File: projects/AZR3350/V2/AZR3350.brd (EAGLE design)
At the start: 128 x 80.5 mm, 168 parts, among them IC1 LM2734Y, IC11 74HC125, IC2 LDO-TS1117CW-3V3, IC3 74S08D, IC5 A4988, IC6 A4988, IC7 A4988, IC8 A4988, IC9 SI87XXIS, J107 ZX62-AB-5PA, Q1 FDS6890A, Q2 IRF520, Q3 IRF520, X3 MSTBV4

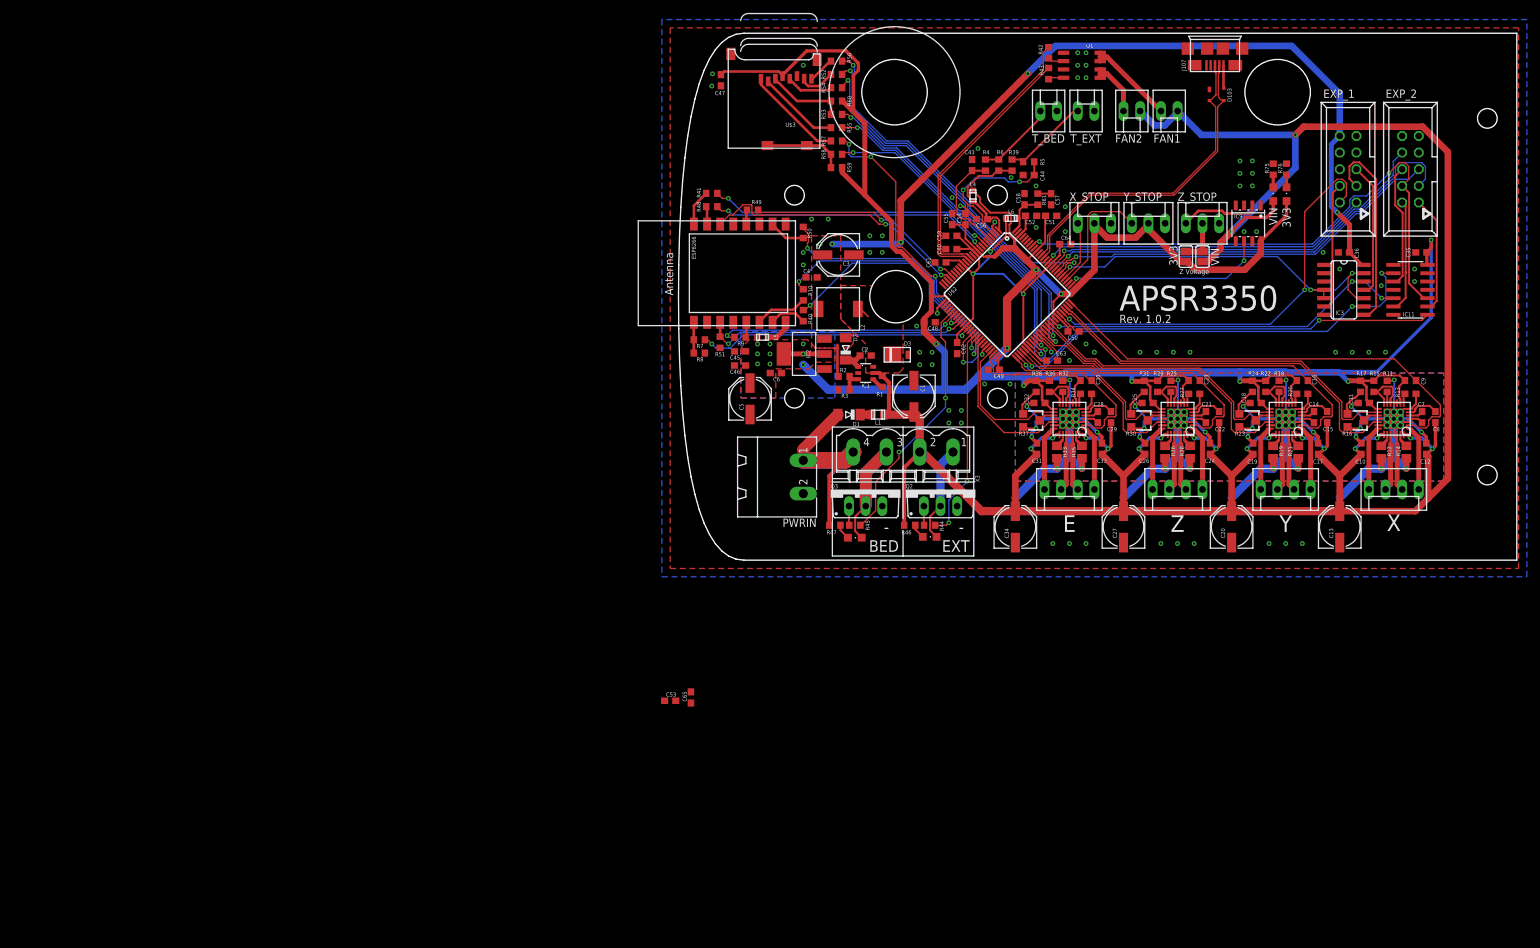
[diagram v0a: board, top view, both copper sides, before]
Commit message: Found all of the parts on DigiKey
(and replaced most that didn't work, for various reasons)
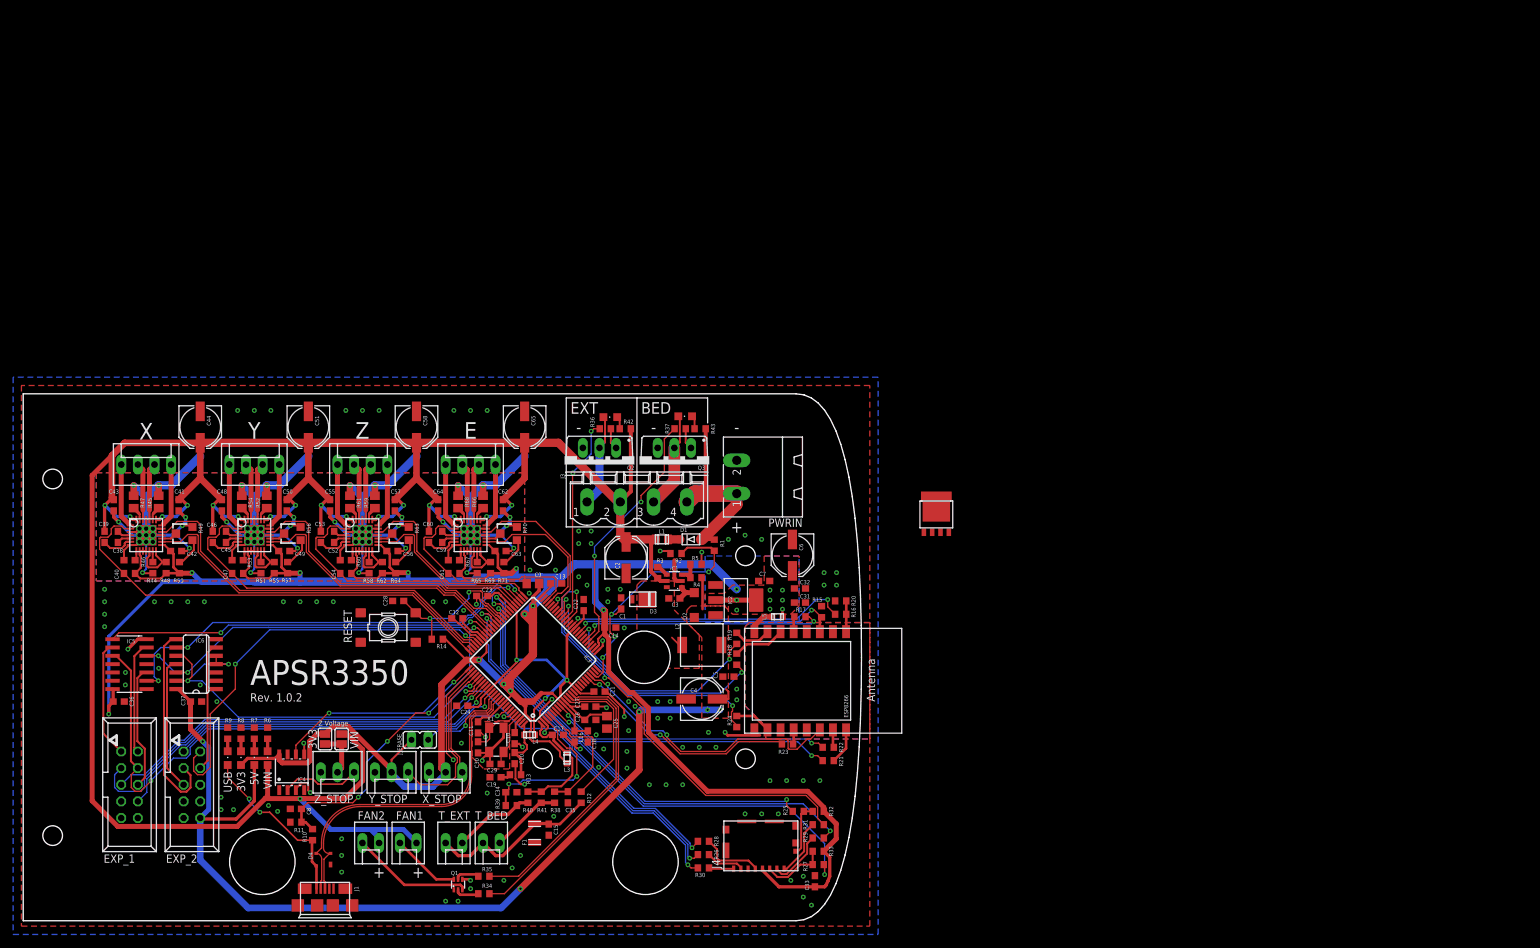
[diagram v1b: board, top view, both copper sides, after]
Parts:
- removed D103: PRTR5V0U2XB, Arduino:SOT143B
- removed IC11: 74HC125, misc:SO14
- removed J107: ZX62-AB-5PA, Arduino:USB-MICRO-10103594
- removed L6: 10uH 100MHz, Zero_V1.0:C0603
- removed R75: 4K7, resistor:R0603
- removed R76: 180R, resistor:R0603
- removed U$2: ATSAM4S8C, misc:LQFP100
- removed U$3: MICROSD, adafruit:MICROSD
- removed X3: MSTBV4, con-phoenix-508:MSTBV4
- added 5V, USB: (no value), led:CHIPLED_0805
- added C37, C38, C39, C41: 100n, resistor:C0603
- added C40, C42: 220n, resistor:C0603
- added D4: PRTR5V0U2XB, Arduino:SOT143B
- added F1: MC36207, misc:MC36207
- added IC10: A4988, RepRapjr:QFN28-TP
- added IC4: SI87XXIS, misc:SOIC08-FAIRCHILD
- added J1: ZX62-AB-5PA, Arduino:USB-MICRO-10103594
- added J3: MSTBV4, con-phoenix-508:MSTBV4
- added J4: MOLEX-105162-001, misc:MOLEX-105162
- added J_ERASE: (no value), jumper:JP1
- added L3: 10uH 100MHz, Zero_V1.0:C0603
- added Q4: BUK9Y53-100B, misc:SOT-669
- added R62, R69: 100K, resistor:R0603
- added R63, R70: 10K, resistor:RTRIM3103
- added R64, R71: 20K, resistor:R0603
- added R65, R67: 10K, resistor:R0603
- added R66, R68: 0R2, resistor:R0805
- added RESET: (no value), Zero_V1.0:TS42_4PINS
- added X1: 12MHz, misc:5.0X3.2_KX-9A
- C1: value 10uF -> 10n; device resistor:PANASONIC_D -> resistor:C0603
- C11, C16, C23: value 220n -> 100n
- C13, C20: value 100u -> 100n; device resistor:PANASONIC_D -> resistor:C0603
- C15, C36: value 100n -> 2.2u
- C18, C32: value 220n -> 10u
- C19: value 100n -> 4u7
- C2: value 10n -> 10uF; device resistor:C0603 -> resistor:PANASONIC_D
- C25, C9: value 220n -> 10u; device resistor:C0603 -> resistor:C0805
- C27: value 100u -> 2.2u 0.1-10ohm ESR; device resistor:PANASONIC_D -> resistor:C0603
- C28: value 100n -> 10n
- C29: value 100n -> 10p
- C3: value 47u -> 100n; device resistor:PANASONIC_D -> resistor:C0603
- C30: value 220n -> 10p
- C31: value 100n -> 10u
- C33: value 100n -> 2K2
- C34: value 100u -> 2.2u; device resistor:PANASONIC_D -> resistor:C0603
- C4: value 4.7uF -> 47u; device resistor:C0603 -> resistor:PANASONIC_D
- C43: value 2.2u -> 100n
- C44: value 2.2u -> 100u; device resistor:C0603 -> resistor:PANASONIC_D
- C45, C46, C53, C55: value 10u -> 100n
- C47: value 2K2 -> 220n
- C49, C54, C56, C61, C63: value 100n -> 220n
- C5: value 10uF -> 4.7uF; device resistor:PANASONIC_D -> resistor:C0603
- C51, C58: value 100n -> 100u; device resistor:C0603 -> resistor:PANASONIC_D
- C57: value 4u7 -> 100n
- C6: value 4.7uF -> 10uF; device resistor:C0603 -> resistor:PANASONIC_D
- C60: value 2.2u 0.1-10ohm ESR -> 100n
- C65: value 10u -> 100u; device resistor:C0603 -> resistor:PANASONIC_D
- C7: value 100n -> 4.7uF
- D1: device Diodi:MINIMELF -> adafruit:SOD-123FL
- D2: device Diodi:MINIMELF -> diode:SOD123
- IC3: value 74S08D -> ATSAM4S8C; device 74xx-us:SO14 -> misc:LQFP100
- IC5: value A4988 -> 74HC125; device RepRapjr:QFN28-TP -> misc:SO14
- IC6: value A4988 -> 74S08D; device RepRapjr:QFN28-TP -> 74xx-us:SO14
- IC9: value SI87XXIS -> A4988; device misc:SOIC08-FAIRCHILD -> RepRapjr:QFN28-TP
- Q1: value FDS6890A -> NX138BKS; device transistor-power:M08A -> misc:SOT363_PHILIPS
- R1: value 10k -> 47K
- R10: value 47R -> 27K
- R11: value 10K -> 47K
- R12, R14, R33: value 0R2 -> 10K; device resistor:R0805 -> resistor:R0603
- R13: value 10K -> 1R
- R15: value 100K -> 4K7
- R16: value 10K -> 470R; device resistor:RTRIM3103 -> resistor:R0603
- R17: value 20K -> 47R
- R18: value 10K -> 47R
- R19: value 0R2 -> 47R; device resistor:R0805 -> resistor:R0603
- R2: value 52.3k -> 4K7
- R20: value 10K -> 2K2
- R21: value 0R2 -> 2K2; device resistor:R0805 -> resistor:R0603
- R22: value 100K -> 470R
- R23: value 10K -> 2K2; device resistor:RTRIM3103 -> resistor:R0603
- R24: value 20K -> 2K2
- R25, R27: value 10K -> 220R
- R26: value 0R2 -> 220R; device resistor:R0805 -> resistor:R0603
- R28: value 0R2 -> 100R; device resistor:R0805 -> resistor:R0603
- R29: value 100K -> 220R
- R3: value 10k -> 100k
- R30: value 10K -> 220R; device resistor:RTRIM3103 -> resistor:R0603
- R31: value 20K -> 220R
- R34: value 10K -> 1K
- R35: value 0R2 -> 1K; device resistor:R0805 -> resistor:R0603
- R36: value 100K -> 180R
- R37: value 10K -> 180R; device resistor:RTRIM3103 -> resistor:R0603
- R38: value 20K -> 10K
- R39: value 4K7 0.1% -> 10K
- R4: value 10K -> 5.53k
- R40: value 47R -> 4K7 0.1%
- R41: value 2K2 -> 4K7 0.1%
- R42, R43: value 1K -> 4K7
- R44: value 180R -> 10K
- R45: value 180R -> 0R2; device resistor:R0603 -> resistor:R0805
- R46, R51: value 4K7 -> 10K
- R47: value 4K7 -> 0R2; device resistor:R0603 -> resistor:R0805
- R48: value 470R -> 100K
- R49: value 2K2 -> 10K; device resistor:R0603 -> resistor:RTRIM3103
- R5: value 10K -> 10k
- R50: value 2K2 -> 20K
- R52: value 220R -> 0R2; device resistor:R0603 -> resistor:R0805
- R53, R58: value 220R -> 10K
- R54: value 100R -> 0R2; device resistor:R0603 -> resistor:R0805
- R55: value 220R -> 100K
- R56: value 220R -> 10K; device resistor:R0603 -> resistor:RTRIM3103
- R57: value 220R -> 20K
- R59: value 10K -> 0R2; device resistor:R0603 -> resistor:R0805
- R6: value 4K7 0.1% -> 4K7
- R61: value 1R -> 0R2; device resistor:R0603 -> resistor:R0805
- R7: value 470R -> 2K2
- R8: value 2K2 -> 180R
- R9: value 47R -> 2K2
- moved EXP_1 208.4 mm to (-83.8, -34.3), turned to 270 degrees
- moved EXP_2 208.4 mm to (-74.3, -34.3), turned to 270 degrees
- moved C36 199.2 mm to (-85.5, -21.6), turned to 0 degrees
- moved IC5 196.6 mm to (-83.8, -15.9), turned to 90 degrees
- moved X 190.5 mm to (-81.3, 14.6), turned to 0 degrees
- moved C8 184.0 mm to (-58.4, -38.0), turned to 0 degrees
- moved 3V3 181.4 mm to (-66.8, -30.2)
- moved R11 179.4 mm to (-58.4, -40.0), turned to 180 degrees
- moved VIN 176.0 mm to (-62.7, -30.2)
- moved IC6 170.5 mm to (-73.7, -15.9), turned to 90 degrees
- moved FAN1 161.2 mm to (-41.3, -43.2)
- moved FAN2 161.2 mm to (-47.0, -43.2)
- moved IC7 158.5 mm to (-81.3, 3.81), turned to 0 degrees
- moved Y 157.5 mm to (-64.8, 14.6), turned to 0 degrees
- moved Q1 157.2 mm to (-33.7, -49.5), turned to 0 degrees
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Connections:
- removed net EN: IC1.4, R1.2
- removed net N$19: R58.2, R59.1, U$3.CD1, U$3.CD2
- removed net N$33: R75.1, VIN.C
- removed net N$34: 3V3.C, R76.1
- new net 24V_LED: R6.1, VIN.C
- new net 3V3_LED: 3V3.C, R8.1
- new net 5V_LED: 5V.C, R7.1
- new net CARDDETECT: J4.P9, R25.2, R32.1
- new net ERASE: IC3.87, J_ERASE.2
- new net PWR_FAIL_DET: C1.1, IC3.23, R1.1, R2.2
- new net SHDN: IC1.4, R3.2
- new net USB_LED: R9.1, USB.C
- new net USB_PWR_MON: C8.2, IC3.68, R10.2, R11.1
- new net VSSA: C15.1, F1.1, R12.2, T_BED.2, T_EXT.2
- new net VSSA_MON: IC3.12, R12.1
- new net XIN: C29.1, IC3.97, X1.3
- new net XOUT: C30.1, IC3.96, X1.1
- net +24V: now also C2.+, C39.2, C41.1, C43.1, C44.+, C46.2, C48.1, C50.1, C51.+, C53.2, C55.1, C57.1, C58.+, C60.2, C62.1, C64.1, C65.+, IC10.22, IC10.28, IC9.22, IC9.28, J3.2, R3.1, R42.2; no longer C1.+, C10.1, C12.1, C13.+, C15.2, C17.1, C19.1, C20.+, C22.2, C24.1, C26.1, C27.+, C29.2, C31.1, C33.1, C34.+, C8.2, IC5.22, IC5.28, IC6.22, IC6.28, R1.1, R46.2, X3.2
- net +3V3: now also C10.2, C11.2, C12.2, C13.2, C14.2, C16.1, C31.1, C33.1, C36.1, C42.1, C49.1, C56.1, C6.+, C63.1, C7.2, C9.2, IC10.10, IC10.11, IC10.15, IC10.9, IC3.10, IC3.27, IC3.50, IC3.69, IC3.91, IC3.98, IC4.8, IC5.14, IC9.10, IC9.11, IC9.15, IC9.9, J4.P4, J_ERASE.1, L3.2, R14.2, R32.2, R33.2, R46.2, R48.2, R50.2, R53.2, R55.2, R57.2, R62.2, R64.2, R67.2, R69.2, R71.2; no longer C11.1, C25.1, C35.1, C45.1, C46.1, C47.1, C48.2, C49.2, C5.+, C50.2, C51.2, C52.2, C53.2, C54.1, C55.1, C6.2, IC11.14, IC5.10, IC5.11, IC5.15, IC5.9, IC6.10, IC6.11, IC6.15, IC6.9, IC9.8, L4.2, R13.2, R15.2, R17.2, R20.2, R22.2, R24.2, R27.2, R29.2, R31.2, R34.2, R36.2, R38.2, R59.2, U$2.10, U$2.27, U$2.50, U$2.69, U$2.91, U$2.98, U$3.4
- net +5V: now also 5V.A, C37.1, C4.+, C5.1, EXP_2.10, IC6.14, R4.1; no longer C3.+, C36.1, C4.1, EXP_1.10, IC3.14, R2.1
- net ADVREF: now also C17.1, IC3.1, L3.1, R40.2, R41.2; no longer C56.1, L4.1, R39.2, R6.2, U$2.1
- net BED: now also IC3.30, R37.1; no longer R45.1, U$2.30
- net BEEPER: now also EXP_2.1, IC3.86; no longer EXP_1.1, U$2.86
- net BOOST: now also C3.1; no longer C2.1
- net BTN_EN1: now also EXP_1.5, IC3.82; no longer EXP_2.5, U$2.82
- net BTN_EN2: now also EXP_1.3, IC3.83; no longer EXP_2.3, U$2.83
- net BTN_ENC: now also EXP_2.2, IC3.71; no longer EXP_1.2, U$2.71
- net CP1E: now also C59.1, IC10.4; no longer C28.1, IC8.4
- net CP1X: now also C38.1, IC7.4; no longer C7.1, IC5.4
- net CP1Y: now also C45.1, IC8.4; no longer C14.1, IC6.4
- net CP1Z: now also C52.1, IC9.4; no longer C21.1, IC7.4
- net CP2E: now also C59.2, IC10.5; no longer C28.2, IC8.5
- net CP2X: now also C38.2, IC7.5; no longer C7.2, IC5.5
- net CP2Y: now also C45.2, IC8.5; no longer C14.2, IC6.5
- net CP2Z: now also C52.2, IC9.5; no longer C21.2, IC7.5
- net EDR_CONN: now also R23.2; no longer R49.2
- net EMOT1A: now also IC10.24; no longer IC8.24
- net EMOT1B: now also IC10.21; no longer IC8.21
- net EMOT2A: now also IC10.26; no longer IC8.26
- net EMOT2B: now also IC10.1; no longer IC8.1
- net ESP_CS: now also R24.2; no longer R50.2
- net ESP_DATA_RDY: now also IC3.21, R23.1; no longer R49.1, U$2.21
- net ESP_EN: now also IC3.34, R15.1; no longer R51.1, U$2.34
- net ESP_MISO: now also R18.1; no longer R10.1
- net ESP_MOSI: now also R19.1; no longer R40.1
- net ESP_RESET: now also R16.2, R20.2; no longer R7.2, R8.2
- net ESP_RST: now also IC3.37, R16.1; no longer R7.1, U$2.37
- net ESP_SPCK: now also R17.1; no longer R9.1
- net ESP_URDX: now also R21.2; no longer R41.2
- net ESP_UTDX: now also R22.2; no longer R48.2
- net E_DIR: now also IC10.19, IC3.43; no longer IC8.19, U$2.43
- net E_EN: now also IC10.2, IC3.48, R67.1; no longer IC8.2, R34.1, U$2.48
- net E_STEP: now also IC10.16, IC3.47; no longer IC8.16, U$2.47
- net FAN1: now also IC3.14, R34.1; no longer R42.1, U$2.14
- net FAN2: now also IC3.13, R35.1; no longer R43.1, U$2.13
- net FB: now also R4.2, R5.1; no longer R2.2, R3.1
- net GND: now also C1.2, C10.1, C11.1, C12.1, C13.1, C14.1, C15.2, C2.-, C20.2, C21.2, C22.2, C27.2, C28.2, C29.2, C34.2, C37.2, C4.-, C40.2, C41.2, C42.2, C44.-, C48.2, C49.2, C5.2, C50.2, C51.-, C58.-, C6.-, C65.-, C7.1, C8.1, C9.1, D4.1, F1.2, IC10.18, IC10.20, IC10.25, IC10.3, IC10.7, IC10.PAD, IC3.26, IC3.45, IC3.61, IC3.70, IC3.77, IC3.95, IC4.3, IC4.5, IC5.1, IC5.12, IC5.13, IC5.4, IC6.1, IC6.2, IC9.18, IC9.20, IC9.25, IC9.7, IC9.PAD, J1.GND, J4.G1, J4.G2, J4.G3, J4.G4, J4.P6, Q1.4, R15.2, R2.1, R20.1, R44.2, R45.1, R47.1, R49.3, R5.2, R52.1, R54.1, R56.3, R58.2, R59.1, R6.2, R61.1, R63.3, R65.2, R66.1, R68.1, R7.2, R70.3, R8.2, R9.2, RESET.4, X1.2, X1.4; no longer C1.-, C10.2, C11.2, C12.2, C13.-, C20.-, C27.-, C3.-, C34.-, C4.2, C44.2, C45.2, C46.2, C48.1, C49.1, C5.-, C50.1, C51.1, C52.1, C53.1, C58.2, C59.2, C6.1, C60.2, C65.2, C9.2, D103.1, IC11.1, IC11.12, IC11.13, IC11.4, IC11.7, IC3.1, IC3.7, IC5.18, IC5.20, IC5.25, IC5.3, IC5.PAD, IC6.18, IC6.20, IC6.25, IC6.3, IC6.PAD, IC9.5, J107.GND, Q1.3, R12.1, R14.1, R16.3, R18.2, R19.1, R21.1, R23.3, R25.2, R26.1, R28.1, R3.2, R30.3, R32.2, R33.1, R35.1, R37.3, R75.2, R76.2, R8.1, T_BED.2, T_EXT.2, U$2.2, U$2.26, U$2.45, U$2.61, U$2.70, U$2.95, U$3.6, U$3.MT1, U$3.MT2
- net HOTEND: now also IC3.40, R36.1; no longer R44.1, U$2.40
- net LCD_CS: now also IC3.80, IC6.10, IC6.13, IC6.4, IC6.5; no longer IC3.10, IC3.13, IC3.4, IC3.5, U$2.80
- net LCD_CS_BUF: now also EXP_2.4, IC6.6; no longer EXP_1.4, IC3.6
- net LCD_MISO: now also IC3.53, IC5.8; no longer IC11.8, U$2.53
- net LCD_MISO_BUF: now also EXP_1.1, IC5.9; no longer EXP_2.1, IC11.9
- net LCD_MOSI: now also IC3.52, IC5.2, IC6.9; no longer IC11.2, IC3.9, U$2.52
- net LCD_MOSI_BUF: now also EXP_2.3, IC6.8; no longer EXP_1.3, IC3.8
- net LCD_RST: now also EXP_1.8, IC3.84; no longer EXP_2.8, U$2.84
- net LCD_SCK: now also IC3.67, IC5.5, IC6.12; no longer IC11.5, IC3.12, U$2.67
- net LCD_SCK_BUF: now also EXP_2.5, IC6.11; no longer EXP_1.5, IC3.11
- net LCD_SD_CS: now also EXP_1.4, IC3.93, IC5.10; no longer EXP_2.4, IC11.10, U$2.93
- net MCCDA: now also IC3.59, R27.1; no longer R53.1, U$2.59
- net MCCK: now also IC3.63, R28.1; no longer R54.1, U$2.63
- net MCDA0: now also IC3.64, R26.1; no longer R52.1, U$2.64
- net MCDA1: now also IC3.81, R30.1; no longer R56.1, U$2.81
- net MCDA2: now also IC3.39, R31.1; no longer R57.1, U$2.39
- net MCDA3: now also IC3.57, R29.1; no longer R55.1, U$2.57
- net MISO: now also IC3.41, R18.2; no longer R10.2, U$2.41
- net MOSI: now also IC3.33, R19.2; no longer R40.2, U$2.33
- net N$13: now also R34.2; no longer R42.2
- net N$18: now also Q1.5, R35.2; no longer Q1.4, R43.2
- net N$20: now also R36.2; no longer R44.2
- net N$21: now also Q1.3; no longer Q1.5, Q1.6
- net N$22: now also Q1.6; no longer Q1.7, Q1.8
- net N$23: now also J3.1; no longer X3.1
- net N$24: now also J3.3; no longer X3.3
- net N$25: now also R37.2; no longer R45.2
- net N$26: now also R42.1; no longer R46.1
- net N$27: now also R43.1; no longer R47.1
- net N$28: now also J4.P7, R26.2; no longer R52.2, U$3.7
- net N$29: now also J4.P3, R27.2, R33.1; no longer R53.2, R60.1, U$3.3
- net N$30: now also J4.P5, R28.2; no longer R54.2, U$3.5
- net N$31: now also J4.P2, R29.2; no longer R55.2, U$3.2
- net N$32: now also J4.P8, R30.2; no longer R56.2, U$3.8
- net N$35: now also J4.P1, R31.2; no longer R57.2, U$3.1
- net N$37: now also C19.1, R13.1; no longer C57.1, R61.1
- net NPCS0: now also IC3.42, R24.1; no longer R50.1, U$2.42
- net NRST: now also C28.1, IC3.60, R14.1, RESET.2; no longer U$2.60
- net REFE: now also IC10.17, R70.2; no longer IC8.17, R37.2
- net REFE-IN: now also R70.1, R71.1; no longer R37.1, R38.1
- net REFX: now also IC7.17, R49.2; no longer IC5.17, R16.2
- net REFX-IN: now also R49.1, R50.1; no longer R16.1, R17.1
- net REFY: now also IC8.17, R56.2; no longer IC6.17, R23.2
- net REFY-IN: now also R56.1, R57.1; no longer R23.1, R24.1
- net REFZ: now also IC9.17, R63.2; no longer IC7.17, R30.2
- net REFZ-IN: now also R63.1, R64.1; no longer R30.1, R31.1
- net ROSCE: now also IC10.13, R65.1; no longer IC8.13, R32.1
- net ROSCX: now also IC7.13, R44.1; no longer IC5.13, R11.1
- net ROSCY: now also IC8.13, R51.1; no longer IC6.13, R18.1
- net ROSCZ: now also IC9.13, R58.1; no longer IC7.13, R25.1
- net RSTE: now also IC10.12, IC10.14, R69.1; no longer IC8.12, IC8.14, R36.1
- net RSTX: now also IC7.12, IC7.14, R48.1; no longer IC5.12, IC5.14, R15.1
- net RSTY: now also IC8.12, IC8.14, R55.1; no longer IC6.12, IC6.14, R22.1
- net RSTZ: now also IC9.12, IC9.14, R62.1; no longer IC7.12, IC7.14, R29.1
- net SAM_TFR_RDY: now also IC3.22; no longer U$2.22
- net SD_CD: now also IC3.58, R25.1; no longer R58.1, U$2.58
- net SD_MOSI_BUF: now also EXP_1.6, IC5.3; no longer EXP_2.6, IC11.3
- net SD_SCK_BUF: now also EXP_1.2, IC5.6; no longer EXP_2.2, IC11.6
- net SNS1E: now also IC10.23, R66.2; no longer IC8.23, R33.2
- net SNS1X: now also IC7.23, R45.2; no longer IC5.23, R12.2
- net SNS1Y: now also IC8.23, R52.2; no longer IC6.23, R19.2
- net SNS1Z: now also IC9.23, R59.2; no longer IC7.23, R26.2
- net SNS2E: now also IC10.27, R68.2; no longer IC8.27, R35.2
- net SNS2X: now also IC7.27, R47.2; no longer IC5.27, R14.2
- net SNS2Y: now also IC8.27, R54.2; no longer IC6.27, R21.2
- net SNS2Z: now also IC9.27, R61.2; no longer IC7.27, R28.2
- net SPCK: now also IC3.31, R17.2; no longer R9.2, U$2.31
- net SW: now also C3.2; no longer C2.2
- net T_BED: now also C35.1, IC3.5, R38.1; no longer C43.1, R4.1, U$2.5
- net T_BED_IN: now also R38.2, R41.1; no longer R4.2, R6.1
- net T_EXT: now also C34.1, IC3.3, R39.1; no longer C44.1, R5.1, U$2.3
- net T_EXT_IN: now also R39.2, R40.1; no longer R39.1, R5.2
- net URXD1: now also IC3.7, R21.1; no longer R41.1, U$2.7
- net USB_N: now also D4.3, IC3.88, J1.D-; no longer D103.3, J107.D-, U$2.88
- net USB_P: now also D4.2, IC3.89, J1.D+; no longer D103.2, J107.D+, U$2.89
- net UTXD1: now also IC3.9, R22.1; no longer R48.1, U$2.9
- net VBUS: now also D4.4, J1.VBUS, R10.1, USB.A; no longer D103.4, J107.VBUS
- net VCPE: now also C60.1, IC10.6; no longer C29.1, IC8.6
- net VCPX: now also C39.1, IC7.6; no longer C8.1, IC5.6
- net VCPY: now also C46.1, IC8.6; no longer C15.1, IC6.6
- net VCPZ: now also C53.1, IC9.6; no longer C22.1, IC7.6
- net VDDOUT: now also C21.1, C22.1, C23.1, C24.1, C25.1, C26.1, C27.1, IC3.11, IC3.16, IC3.36, IC3.56, IC3.85, L4.2; no longer C59.1, C60.1, C61.1, C62.1, C63.1, C64.1, C65.1, L6.2, U$2.11, U$2.16, U$2.36, U$2.56, U$2.85
- net VDDPLL: now also C20.1, IC3.100, L4.1, R13.2; no longer C58.1, L6.1, R61.2, U$2.100
- net VIN: now also J3.4, R1.2, R43.2; no longer R47.2, X3.4
- net VREGE: now also C61.1, IC10.8; no longer C30.1, IC8.8
- net VREGX: now also C40.1, IC7.8; no longer C9.1, IC5.8
- net VREGY: now also C47.1, IC8.8; no longer C16.1, IC6.8
- net VREGZ: now also C54.1, IC9.8; no longer C23.1, IC7.8
- net XMOT1A: now also IC7.24; no longer IC5.24
- net XMOT1B: now also IC7.21; no longer IC5.21
- net XMOT2A: now also IC7.26; no longer IC5.26
- net XMOT2B: now also IC7.1; no longer IC5.1
- net X_DIR: now also IC3.72, IC7.19; no longer IC5.19, U$2.72
- net X_EN: now also IC3.75, IC7.2, R46.1; no longer IC5.2, R13.1, U$2.75
- net X_STEP: now also IC3.73, IC7.16; no longer IC5.16, U$2.73
- net X_STOP: now also IC3.79; no longer U$2.79
- net YMOT1A: now also IC8.24; no longer IC6.24
- net YMOT1B: now also IC8.21; no longer IC6.21
- net YMOT2A: now also IC8.26; no longer IC6.26
- net YMOT2B: now also IC8.1; no longer IC6.1
- net Y_DIR: now also IC3.62, IC8.19; no longer IC6.19, U$2.62
- net Y_EN: now also IC3.66, IC8.2, R53.1; no longer IC6.2, R20.1, U$2.66
- net Y_STEP: now also IC3.65, IC8.16; no longer IC6.16, U$2.65
- net Y_STOP: now also IC3.78; no longer U$2.78
- net ZMOT1A: now also IC9.24; no longer IC7.24
- net ZMOT1B: now also IC9.21; no longer IC7.21
- net ZMOT2A: now also IC9.26; no longer IC7.26
- net ZMOT2B: now also IC9.1; no longer IC7.1
- net Z_DIR: now also IC3.51, IC9.19; no longer IC7.19, U$2.51
- net Z_EN: now also IC3.55, IC9.2, R60.1; no longer IC7.2, R27.1, U$2.55
- net Z_STEP: now also IC3.54, IC9.16; no longer IC7.16, U$2.54
- net Z_STOP: now also IC3.76, IC4.6; no longer IC9.6, U$2.76
- net Z_STOP_IN: now also IC4.2; no longer IC9.2
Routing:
- net GND: track 295.6 -> 370.1 mm, vias 136 -> 183
- net USB_PWR_MON: track 0.00 -> 50.1 mm, vias 0 -> 4
- net PWR_FAIL_DET: track 0.00 -> 40.6 mm, vias 0 -> 4
- net +3V3: track 441.2 -> 471.1 mm, vias 18 -> 20
- net VSSA: track 0.00 -> 26.6 mm
- net MCCDA: track 51.4 -> 77.4 mm
- net VBUS: track 3.52 -> 26.9 mm, vias 0 -> 2
- net MCDA3: track 52.5 -> 75.6 mm
- net VSSA_MON: track 0.00 -> 22.5 mm
- net +5V: track 130.5 -> 152.2 mm
- net NRST: track 3.49 -> 24.2 mm, vias 1 -> 2
- net SD_CD: track 53.5 -> 70.3 mm
- net MCDA2: track 52.1 -> 68.6 mm, vias 4 -> 2
- net ERASE: track 0.00 -> 14.3 mm, vias 0 -> 1
- net N$19: track 12.3 -> 0.00 mm
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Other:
- outline, holes or cut-outs redrawn
- board text added: "+"

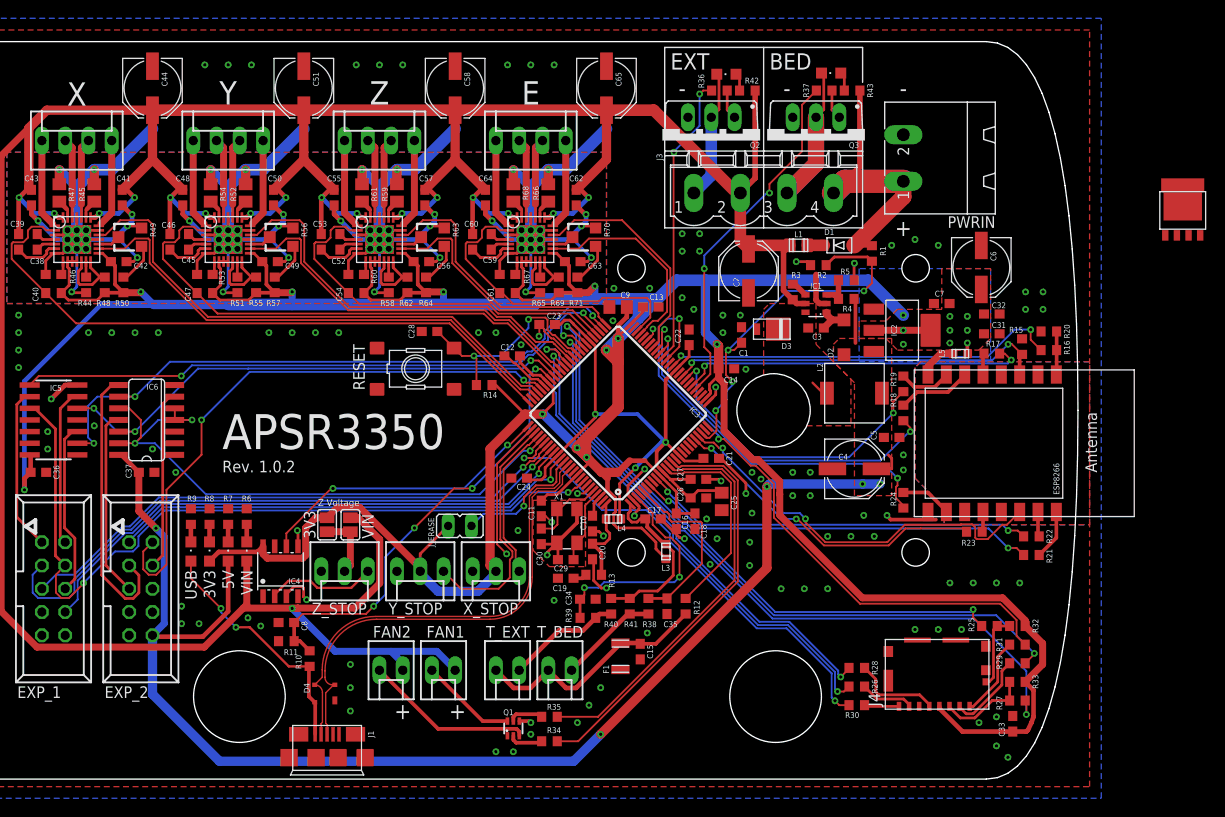
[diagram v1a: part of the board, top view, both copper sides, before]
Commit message: Changed out mosfets, other improvements (APSR)
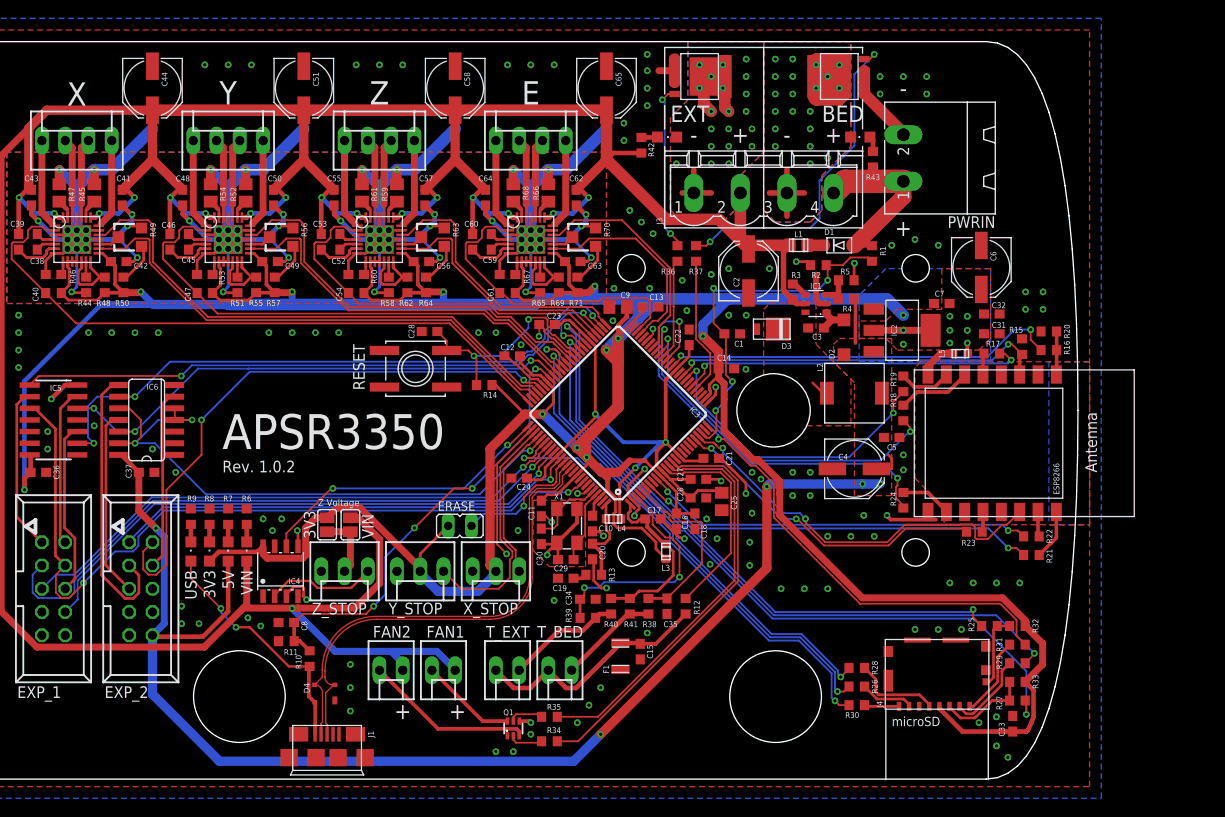
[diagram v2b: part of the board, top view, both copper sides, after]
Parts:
- removed Q4: BUK9Y53-100B, misc:SOT-669
- Q2, Q3: value IRF520 -> BUK9Y53-100B; device transistor-power:TO220BV -> misc:SOT-669
- RESET: device Zero_V1.0:TS42_4PINS -> misc:EVQQ2
- moved R37 22.6 mm to (-13.7, 2.29), turned to 90 degrees
- moved R36 18.4 mm to (-15.7, 2.29), turned to 90 degrees
- moved R42 13.0 mm to (-19.7, 14.1), turned to 270 degrees
- moved EXT_L 9.43 mm to (-16.9, 15.0), turned to 270 degrees
- moved R43 7.83 mm to (5.59, 12.6), turned to 270 degrees
- moved BED_L 7.67 mm to (4.19, 15.0)
- moved Q3 7.43 mm to (1.91, 21.6), turned to 90 degrees
- moved Q2 7.10 mm to (-13.3, 21.6), turned to 270 degrees
- moved C1 1.02 mm to (-9.78, -6.48), turned to 0 degrees
- renumbered J_ERASE to ERASE
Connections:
- net CARDDETECT renamed DET
- net N$1 renamed VIN_F
- net N$10 renamed ESP_VIN
- net N$13 renamed FAN1_G
- net N$18 renamed FAN2_G
- net N$21 renamed FAN2_D
- net N$22 renamed FAN1_D
- net N$26 renamed EXT_L
- net N$27 renamed BED_L
- net N$28 renamed DAT0
- net N$29 renamed CMD
- net N$30 renamed CLK
- net N$31 renamed DAT3
- net N$32 renamed DAT1
- net N$35 renamed DAT2
- removed net N$20: Q2.G, R36.2
- removed net N$23: EXT_L.C, J3.1, Q2.D
- removed net N$24: BED_L.C, J3.3, Q3.D
- removed net N$25: Q3.G, R37.2
- removed net NRST: C28.1, IC3.60, R14.1, RESET.2
- new net BED_D: BED_L.C, J3.3, Q3.EXP, Q3.MB
- new net BED_G: Q3.4, R37.2
- new net EXT_D: EXT_L.C, J3.1, Q2.EXP, Q2.MB
- new net EXT_G: Q2.4, R36.2
- new net RESET: C28.1, IC3.60, R14.1, RESET.A'
- net GND: now also Q2.1, Q2.2, Q2.3, Q3.1, Q3.2, Q3.3, RESET.B, RESET.B'; no longer Q2.S, Q3.S, RESET.4
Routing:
- net BED_G: track 0.00 -> 36.4 mm, vias 0 -> 2
- net RESET: track 0.00 -> 24.8 mm, vias 0 -> 2
- net N$24: track 24.4 -> 0.00 mm
- net NRST: track 24.2 -> 0.00 mm, vias 2 -> 0
- net BED_D: track 0.00 -> 23.9 mm, vias 0 -> 20
- net BED: track 38.8 -> 15.3 mm, vias 2 -> 0
- net HOTEND: track 31.8 -> 11.1 mm, vias 2 -> 0
- net EXT_G: track 0.00 -> 18.2 mm, vias 0 -> 2
- net N$23: track 14.2 -> 0.00 mm
- net EXT_D: track 0.00 -> 14.0 mm, vias 0 -> 20
- net GND: track 370.1 -> 383.6 mm, vias 183 -> 198
- net VIN: track 39.8 -> 29.1 mm
- net +24V: track 387.5 -> 379.7 mm
- net N$25: track 3.25 -> 0.00 mm
- net N$20: track 3.25 -> 0.00 mm
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- added copper zone on layer 1, net BED_D
- added copper zone on layer 16, net BED_D
- added copper zone on layer 1, net EXT_D
- added copper zone on layer 16, net EXT_D
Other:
- board text added: "microSD"
